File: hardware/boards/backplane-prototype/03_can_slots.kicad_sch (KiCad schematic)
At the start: 17 parts, among them J1 SLOT_1, J2 XY308-2.54-3P / EXTERNAL CAN, J3 SLOT_2, J4 SLOT_3, J6 SLOT_4, J7 SLOT_5, J8 SLOT_6, U5 TCAN3413DR

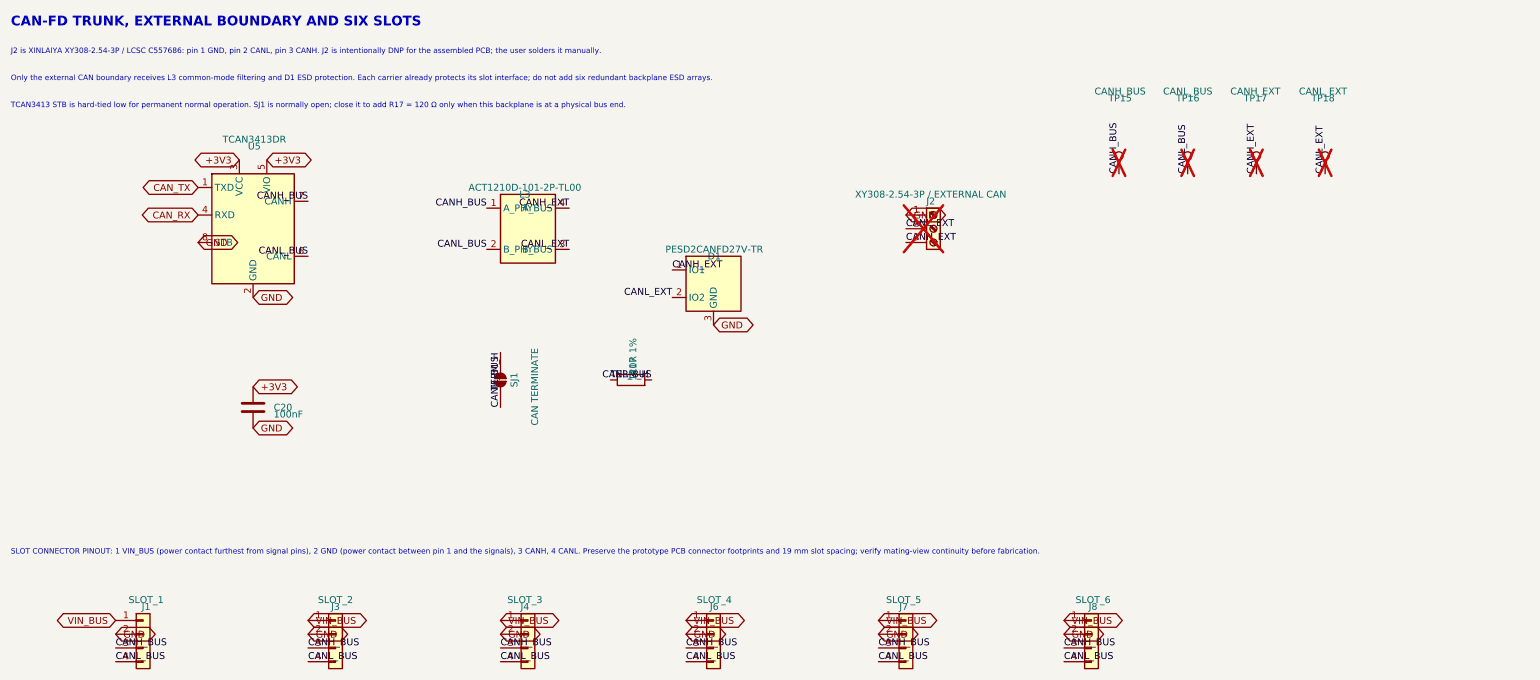
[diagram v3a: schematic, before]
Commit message: hardware: constrain backplane CAN-FD pairs
Rename the external and slot CAN nets to KiCad P/N differential pairs, apply the carrier coupling and skew constraints, and set the 2 oz backplane stackup surface finish to ENIG.
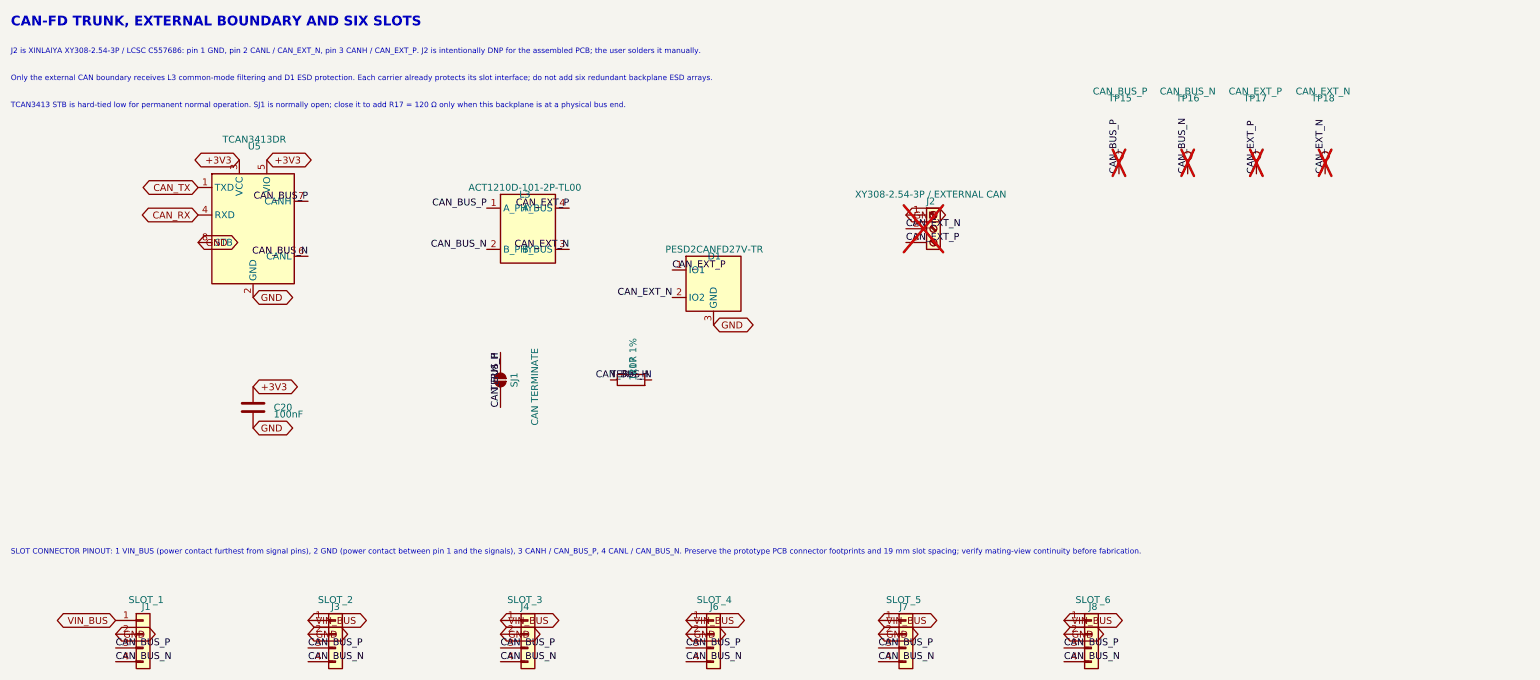
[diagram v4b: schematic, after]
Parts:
- TP15: value CANH_BUS -> CAN_BUS_P
- TP16: value CANL_BUS -> CAN_BUS_N
- TP17: value CANH_EXT -> CAN_EXT_P
- TP18: value CANL_EXT -> CAN_EXT_N
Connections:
- net CANH_BUS renamed CAN_BUS_P
- net CANH_EXT renamed CAN_EXT_P
- net CANL_BUS renamed CAN_BUS_N
- net CANL_EXT renamed CAN_EXT_N
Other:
- note added: "J2 is XINLAIYA XY308-2.54-3P / LCSC C557686: pin 1 GND, pin 2 CANL / CAN_EXT_N, pin 3 CANH / CAN_EXT_P. J2 is intentionally DNP for the assembled PCB; the user solders it manually."
- note added: "SLOT CONNECTOR PINOUT: 1 VIN_BUS (power contact furthest from signal pins), 2 GND (power contact between pin 1 and the signals), 3 CANH / CAN_BUS_P, 4 CANL / CAN_BUS_N. Preserve the prototype PCB connector footprints and 19 mm slot spacing; verify mating-view continuity before fabrication."
- note removed: "J2 is XINLAIYA XY308-2.54-3P / LCSC C557686: pin 1 GND, pin 2 CANL, pin 3 CANH. J2 is intentionally DNP for the assembled PCB; the user solders it manually."
- note removed: "SLOT CONNECTOR PINOUT: 1 VIN_BUS (power contact furthest from signal pins), 2 GND (power contact between pin 1 and the signals), 3 CANH, 4 CANL. Preserve the prototype PCB connector footprints and 19 mm slot spacing; verify mating-view continuity before fabrication."
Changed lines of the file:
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@@
 	(generator_version "10.0")
 	(paper "A4")
-	(text "SLOT CONNECTOR PINOUT: 1 VIN_BUS (power contact furthest from signal pins), 2 GND (power contact between pin 1 and the signals), 3 CANH, 4 CANL. Preserve the prototype PCB connector footprints and 19 mm slot spacing; verify mating-view continuity before fabrication."
+	(text "SLOT CONNECTOR PINOUT: 1 VIN_BUS (power contact furthest from signal pins), 2 GND (power contact between pin 1 and the signals), 3 CANH / CAN_BUS_P, 4 CANL / CAN_BUS_N. Preserve the prototype PCB connector footprints and 19 mm slot spacing; verify mating-view continuity before fabrication."
 		(exclude_from_sim no)
 		(at 20 115 0)
@@
 		)
 	)
-	(text "J2 is XINLAIYA XY308-2.54-3P / LCSC C557686: pin 1 GND, pin 2 CANL, pin 3 CANH. J2 is intentionally DNP for the assembled PCB; the user solders it manually."
+	(text "J2 is XINLAIYA XY308-2.54-3P / LCSC C557686: pin 1 GND, pin 2 CANL / CAN_EXT_N, pin 3 CANH / CAN_EXT_P. J2 is intentionally DNP for the assembled PCB; the user solders it manually."
 		(exclude_from_sim no)
 		(at 20 22.5 0)
@@
 		)
 	)
-	(label "CANL_EXT"
+	(label "CAN_EXT_N"
 		(at 185.42 54.61 0)
 		(effects
@@
 		)
 	)
-	(label "CANH_BUS"
+	(label "CAN_BUS_P"
 		(at 74.93 49.53 180)
 		(effects
@@
 		)
 	)
-	(label "CANL_EXT"
+	(label "CAN_EXT_N"
 		(at 123.19 58.42 180)
 		(effects
@@
 		)
 	)
-	(label "CANL_BUS"
+	(label "CAN_BUS_N"
 		(at 39.37 134.62 0)
 		(effects
@@
 		)
 	)
-	(label "CANH_BUS"
+	(label "CAN_BUS_P"
 		(at 144.78 132.08 0)
 		(effects
@@
 		)
 	)
-	(label "CANL_BUS"
+	(label "CAN_BUS_N"
 		(at 107.95 58.42 180)
 		(effects
@@
 		)
 	)
-	(label "CANH_BUS"
+	(label "CAN_BUS_P"
 		(at 74.93 132.08 0)
 		(effects
@@
 		)
 	)
-	(label "CANH_BUS"
+	(label "CAN_BUS_P"
 		(at 110.49 132.08 0)
 		(effects
@@
 		)
 	)
-	(label "CANL_EXT"
+	(label "CAN_EXT_N"
 		(at 142.24 67.31 180)
 		(effects
@@
 		)
 	)
-	(label "CANL_BUS"
+	(label "CAN_BUS_N"
 		(at 180.34 134.62 0)
 		(effects
@@
 		)
 	)
-	(label "CANH_EXT"
+	(label "CAN_EXT_P"
 		(at 142.24 62.23 0)
 		(effects
@@
 		)
 	)
-	(label "CANH_BUS"
+	(label "CAN_BUS_P"
 		(at 107.95 50.8 180)
 		(effects
@@
 		)
 	)
-	(label "CANH_BUS"
+	(label "CAN_BUS_P"
 		(at 224.79 44.45 90)
 		(effects
@@
 		)
 	)
-	(label "CANH_BUS"
+	(label "CAN_BUS_P"
 		(at 214.63 132.08 0)
 		(effects
@@
 		)
 	)
-	(label "CANL_BUS"
+	(label "CAN_BUS_N"
 		(at 138.43 82.55 180)
 		(effects
@@
 		)
 	)
-	(label "CANL_BUS"
+	(label "CAN_BUS_N"
 		(at 144.78 134.62 0)
 		(effects
@@
 		)
 	)
-	(label "CANH_BUS"
+	(label "CAN_BUS_P"
 		(at 110.49 87.63 90)
 		(effects
@@
 		)
 	)
-	(label "CANL_BUS"
+	(label "CAN_BUS_N"
 		(at 214.63 134.62 0)
 		(effects
@@
 		)
 	)
-	(label "CANH_EXT"
+	(label "CAN_EXT_P"
 		(at 123.19 50.8 180)
 		(effects
@@
 		)
 	)
-	(label "CANH_BUS"
+	(label "CAN_BUS_P"
 		(at 180.34 132.08 0)
 		(effects
@@
 		)
 	)
-	(label "CANL_BUS"
+	(label "CAN_BUS_N"
 		(at 74.93 134.62 0)
 		(effects
@@
 		)
 	)
-	(label "CANL_BUS"
+	(label "CAN_BUS_N"
 		(at 237.49 44.45 90)
 		(effects
@@
 		)
 	)
-	(label "CANL_BUS"
+	(label "CAN_BUS_N"
 		(at 110.49 134.62 0)
 		(effects
@@
 		)
 	)
-	(label "CANL_BUS"
+	(label "CAN_BUS_N"
 		(at 74.93 59.69 180)
 		(effects
@@
 		)
 	)
-	(label "CANL_EXT"
+	(label "CAN_EXT_N"
 		(at 262.89 44.45 90)
 		(effects
@@
 		)
 	)
-	(label "CANH_EXT"
+	(label "CAN_EXT_P"
 		(at 185.42 57.15 0)
 		(effects
@@
 		)
 	)
-	(label "CANH_BUS"
+	(label "CAN_BUS_P"
 		(at 39.37 132.08 0)
 		(effects
@@
 		)
 	)
-	(label "CANH_EXT"
+	(label "CAN_EXT_P"
 		(at 250.19 44.45 90)
 		(effects
@@
 			)
 		)
-		(property "Value" "CANL_BUS"
+		(property "Value" "CAN_BUS_N"
 			(at 237.5 29.21 0)
 			(show_name no)
@@
 			)
 		)
-		(property "Value" "CANL_EXT"
+		(property "Value" "CAN_EXT_N"
 			(at 262.5 29.21 0)
 			(show_name no)
@@
 			)
 		)
-		(property "Value" "CANH_EXT"
+		(property "Value" "CAN_EXT_P"
 			(at 250 29.21 0)
 			(show_name no)
@@
 			)
 		)
-		(property "Value" "CANH_BUS"
+		(property "Value" "CAN_BUS_P"
 			(at 225 29.21 0)
 			(show_name no)

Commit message: checkpoint: save backplane layout updates
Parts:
- removed TP17: CAN_EXT_P, TestPoint:TestPoint_Pad_D1.5mm, symbol Connector:TestPoint
- removed TP18: CAN_EXT_N, TestPoint:TestPoint_Pad_D1.5mm, symbol Connector:TestPoint
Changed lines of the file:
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@@
-		)
-	)
-	(label "CAN_EXT_N"
-		(at 262.89 44.45 90)
-		(effects
-			(font
-				(size 1.27 1.27)
-			)
-			(justify left bottom)
 		)
 	)
@@
 	(label "CAN_BUS_P"
 		(at 39.37 132.08 0)
-		(effects
-			(font
-				(size 1.27 1.27)
-			)
-			(justify left bottom)
-		)
-	)
-	(label "CAN_EXT_P"
-		(at 250.19 44.45 90)
 		(effects
 			(font
@@
 	)
 	(symbol
-		(lib_id "Connector:TestPoint")
-		(at 262.89 44.45 0)
-		(unit 1)
-		(body_style 1)
-		(exclude_from_sim no)
-		(in_bom no)
-		(on_board yes)
-		(in_pos_files yes)
-		(dnp yes)
-		(property "Reference" "TP18"
-			(at 262.5 30.48 0)
-			(show_name no)
-			(do_not_autoplace no)
-			(effects
-				(font
-					(size 1.27 1.27)
-				)
-			)
-		)
-		(property "Value" "CAN_EXT_N"
-			(at 262.5 29.21 0)
-			(show_name no)
-			(do_not_autoplace no)
-			(effects
-				(font
-					(size 1.27 1.27)
-				)
-			)
-		)
-		(property "Footprint" "TestPoint:TestPoint_Pad_D1.5mm"
-			(at 267.58 45 0)
-			(hide yes)
-			(show_name no)
-			(do_not_autoplace no)
-			(effects
-				(font
-					(size 1.27 1.27)
-				)
-			)
-		)
-		(property "Datasheet" ""
-			(at 267.58 45 0)
-			(hide yes)
-			(show_name no)
-			(do_not_autoplace no)
-			(effects
-				(font
-					(size 1.27 1.27)
-				)
-			)
-		)
-		(property "Description" "test point"
-			(at 262.5 45 0)
-			(hide yes)
-			(show_name no)
-			(do_not_autoplace no)
-			(effects
-				(font
-					(size 1.27 1.27)
-				)
-			)
-		)
-		(pin "1"
-		)
-		(instances
-			(project "backplane-prototype"
-				(path "/348cc909-6345-4013-9bef-98714057a65b/eb7e4e77-e42b-4b43-976a-f7a3e8147b95"
-					(reference "TP18")
-					(unit 1)
-				)
-			)
-		)
-	)
-	(symbol
 		(lib_id "backplane-backpack:ACT1210D_1243")
 		(at 115.57 54.61 0)
@@
 					(unit 1)
 				)
-			)
-		)
-	)
-	(symbol
-		(lib_id "Connector:TestPoint")
-		(at 250.19 44.45 0)
-		(unit 1)
-		(body_style 1)
-		(exclude_from_sim no)
-		(in_bom no)
-		(on_board yes)
-		(in_pos_files yes)
-		(dnp yes)
-		(property "Reference" "TP17"
-			(at 250 30.48 0)
-			(show_name no)
-			(do_not_autoplace no)
-			(effects
-				(font
-					(size 1.27 1.27)
-				)
-			)
-		)
-		(property "Value" "CAN_EXT_P"
-			(at 250 29.21 0)
-			(show_name no)
-			(do_not_autoplace no)
-			(effects
-				(font
-					(size 1.27 1.27)
-				)
-			)
-		)
-		(property "Footprint" "TestPoint:TestPoint_Pad_D1.5mm"
-			(at 255.08 45 0)
-			(hide yes)
-			(show_name no)
-			(do_not_autoplace no)
-			(effects
-				(font
-					(size 1.27 1.27)
-				)
-			)
-		)
-		(property "Datasheet" ""
-			(at 255.08 45 0)
-			(hide yes)
-			(show_name no)
-			(do_not_autoplace no)
-			(effects
-				(font
-					(size 1.27 1.27)
-				)
-			)
-		)
-		(property "Description" "test point"
-			(at 250 45 0)
-			(hide yes)
-			(show_name no)
-			(do_not_autoplace no)
-			(effects
-				(font
-					(size 1.27 1.27)
-				)
-			)
-		)
-		(pin "1"
-		)
-		(instances
-			(project "backplane-prototype"
-				(path "/348cc909-6345-4013-9bef-98714057a65b/eb7e4e77-e42b-4b43-976a-f7a3e8147b95"
-					(reference "TP17")
-					(unit 1)
-				)

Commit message: hardware: swap D1 CAN lines and tidy 12V VIN zone
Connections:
- net CAN_EXT_N: now also D1.1 (IO1); no longer D1.2 (IO2)
- net CAN_EXT_P: now also D1.2 (IO2); no longer D1.1 (IO1)
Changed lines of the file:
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@@
 		)
 	)
-	(label "CAN_EXT_N"
+	(label "CAN_EXT_P"
 		(at 142.24 67.31 180)
 		(effects
@@
 		)
 	)
-	(label "CAN_EXT_P"
+	(label "CAN_EXT_N"
 		(at 142.24 62.23 0)
 		(effects
